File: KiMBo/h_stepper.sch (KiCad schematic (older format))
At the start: 24 parts, among them U18 TMC2130

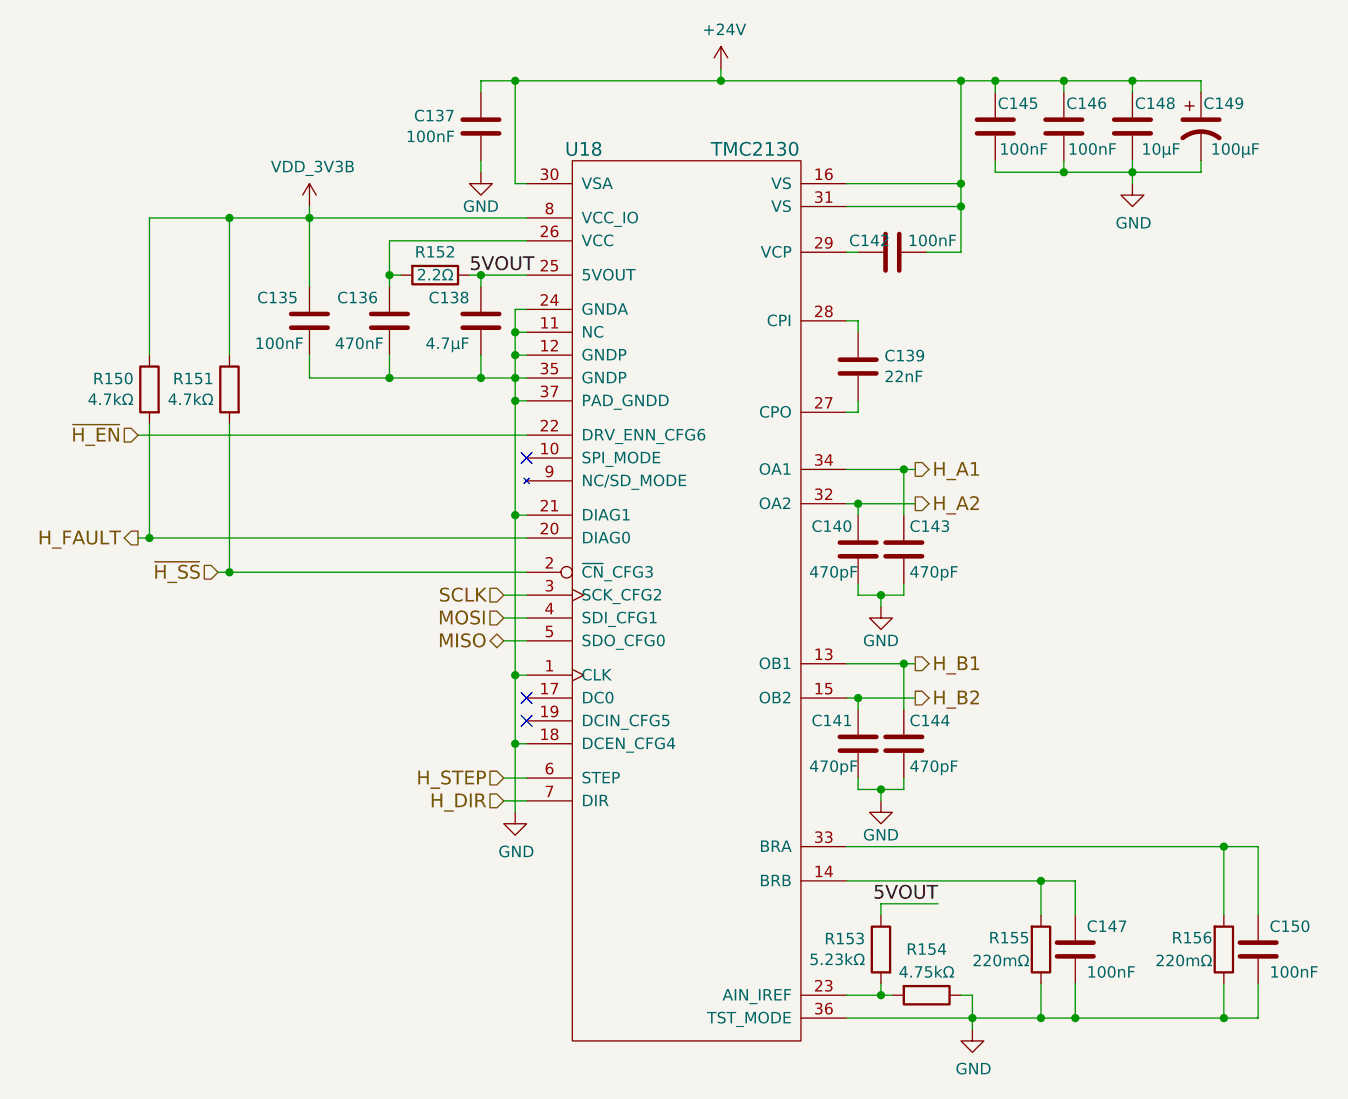
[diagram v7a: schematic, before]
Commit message: Remove the unneeded oscillator, track down which components are underneath the OSD3358 and put them on the top
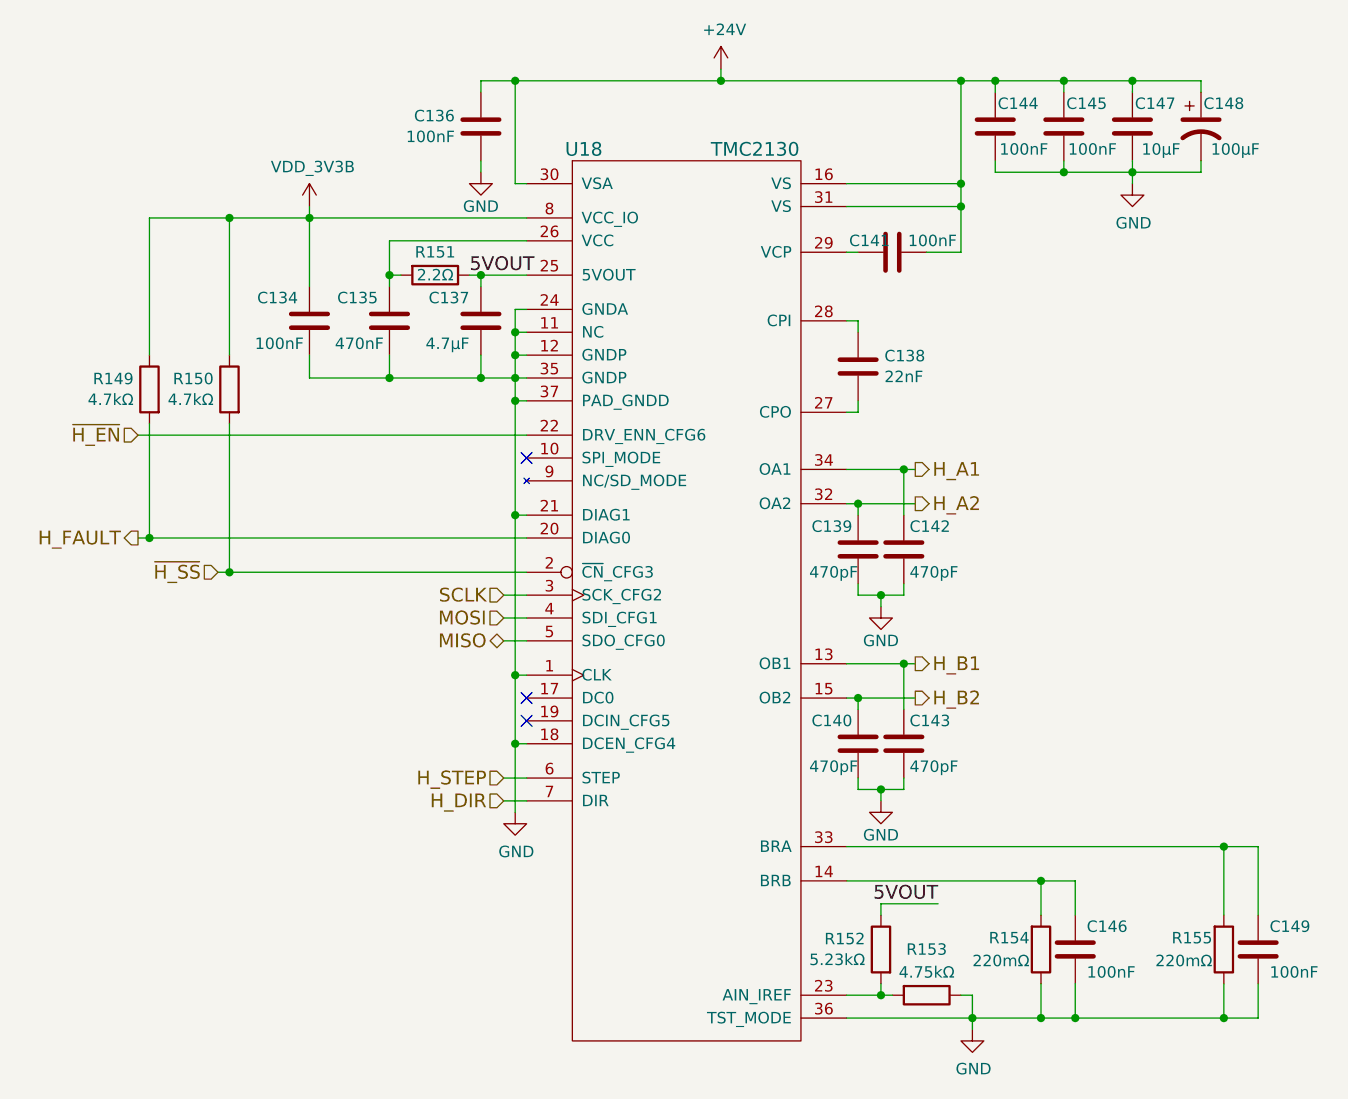
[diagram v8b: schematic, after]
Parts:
- renumbered C135 to C134, C136 to C135, C137 to C136, C138 to C137, C139 to C138, C140 to C139, C141 to C140, C142 to C141, C143 to C142, C144 to C143, C145 to C144, C146 to C145, C147 to C146, C148 to C147, C149 to C148, C150 to C149, R150 to R149, R151 to R150, R152 to R151, R153 to R152, R154 to R153, R155 to R154, R156 to R155
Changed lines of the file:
@@
 MOSI
 $Comp
-L C C137
+L C C136
 U 1 1 5BA7E11E
 P 7300 3950
-F 0 "C137" H 7186 3904 50  0000 R CNN
+F 0 "C136" H 7186 3904 50  0000 R CNN
 F 1 "100nF" H 7186 3995 50  0000 R CNN
 F 2 "Capacitors_SMD:C_0603" H 7338 3800 50  0001 C CNN
@@
 $EndComp
 $Comp
-L C C142
+L C C141
 U 1 1 589B8C70
 P 9100 4500
-F 0 "C142" V 9050 4400 50  0000 C CNN
+F 0 "C141" V 9050 4400 50  0000 C CNN
 F 1 "100nF" V 9050 4675 50  0000 C CNN
 F 2 "Capacitors_SMD:C_0603" H 9138 4350 50  0001 C CNN
@@
 $EndComp
 $Comp
-L CP1 C149
+L CP1 C148
 U 1 1 589B8CBD
 P 10450 3950
-F 0 "C149" H 10550 4050 50  0000 C CNN
+F 0 "C148" H 10550 4050 50  0000 C CNN
 F 1 "100μF" H 10600 3850 50  0000 C CNN
 F 2 "Capacitors_SMD:c_elec_8x10" H 10450 3950 50  0001 C CNN
@@
 $EndComp
 $Comp
-L C C145
+L C C144
 U 1 1 5BA7E121
 P 9550 3950
-F 0 "C145" H 9450 4050 50  0000 C CNN
+F 0 "C144" H 9450 4050 50  0000 C CNN
 F 1 "100nF" H 9425 3850 50  0000 C CNN
 F 2 "Capacitors_SMD:C_0603" H 9588 3800 50  0001 C CNN
@@
 $EndComp
 $Comp
-L GND #PWR0204
+L GND #PWR0202
 U 1 1 5BA7E122
 P 7300 4150
-F 0 "#PWR0204" H 7300 3900 50  0001 C CNN
+F 0 "#PWR0202" H 7300 3900 50  0001 C CNN
 F 1 "GND" H 7300 4000 50  0000 C CNN
 F 2 "" H 7300 4150 50  0000 C CNN
@@
 $EndComp
 $Comp
-L C C146
+L C C145
 U 1 1 5BA7E123
 P 9850 3950
-F 0 "C146" H 9750 4050 50  0000 C CNN
+F 0 "C145" H 9750 4050 50  0000 C CNN
 F 1 "100nF" H 9725 3850 50  0000 C CNN
 F 2 "Capacitors_SMD:C_0603" H 9888 3800 50  0001 C CNN
@@
 $EndComp
 $Comp
-L GND #PWR0205
+L GND #PWR0203
 U 1 1 5BA7E124
 P 10150 4200
-F 0 "#PWR0205" H 10150 3950 50  0001 C CNN
+F 0 "#PWR0203" H 10150 3950 50  0001 C CNN
 F 1 "GND" H 10155 4027 50  0000 C CNN
 F 2 "" H 10150 4200 50  0000 C CNN
@@
 $EndComp
 $Comp
-L +24V #PWR0206
+L +24V #PWR0204
 U 1 1 589BEDE1
 P 8350 3700
-F 0 "#PWR0206" H 8350 3550 50  0001 C CNN
+F 0 "#PWR0204" H 8350 3550 50  0001 C CNN
 F 1 "+24V" H 8365 3873 50  0000 C CNN
 F 2 "" H 8350 3700 50  0000 C CNN
@@
 $EndComp
 $Comp
-L C C139
+L C C138
 U 1 1 5BA7E126
 P 8950 5000
-F 0 "C139" H 9065 5046 50  0000 L CNN
+F 0 "C138" H 9065 5046 50  0000 L CNN
 F 1 "22nF" H 9065 4955 50  0000 L CNN
 F 2 "Capacitors_SMD:C_0603" H 8988 4850 50  0001 C CNN
@@
 $EndComp
 $Comp
-L R R156
+L R R155
 U 1 1 5BA7E127
 P 10550 7550
-F 0 "R156" H 10500 7500 50  0000 R CNN
+F 0 "R155" H 10500 7500 50  0000 R CNN
 F 1 "220mΩ" H 10500 7600 50  0000 R CNN
 F 2 "Resistors_SMD:R_0805" V 10480 7550 50  0001 C CNN
@@
 $EndComp
 $Comp
-L R R155
+L R R154
 U 1 1 5BA7E128
 P 9750 7550
-F 0 "R155" H 9700 7500 50  0000 R CNN
+F 0 "R154" H 9700 7500 50  0000 R CNN
 F 1 "220mΩ" H 9700 7600 50  0000 R CNN
 F 2 "Resistors_SMD:R_0805" V 9680 7550 50  0001 C CNN
@@
 $EndComp
 $Comp
-L GND #PWR0207
+L GND #PWR0205
 U 1 1 589C2B70
 P 9450 7900
-F 0 "#PWR0207" H 9450 7650 50  0001 C CNN
+F 0 "#PWR0205" H 9450 7650 50  0001 C CNN
 F 1 "GND" H 9455 7727 50  0000 C CNN
 F 2 "" H 9450 7900 50  0000 C CNN
@@
 NoConn ~ 7500 6450
 $Comp
-L R R152
+L R R151
 U 1 1 589C4ED8
 P 7100 4600
-F 0 "R152" V 7000 4600 50  0000 C CNN
+F 0 "R151" V 7000 4600 50  0000 C CNN
 F 1 "2.2Ω" V 7100 4600 50  0000 C CNN
 F 2 "Resistors_SMD:R_0603" V 7030 4600 50  0001 C CNN
@@
 $EndComp
 $Comp
-L C C136
+L C C135
 U 1 1 5BA7E12C
 P 6900 4800
-F 0 "C136" H 6950 4900 50  0000 L CNN
+F 0 "C135" H 6950 4900 50  0000 L CNN
 F 1 "470nF" H 6925 4700 50  0000 L CNN
 F 2 "Capacitors_SMD:C_0603" H 6938 4650 50  0001 C CNN
@@
 NoConn ~ 7500 6550
 $Comp
-L GND #PWR0208
+L GND #PWR0206
 U 1 1 5BA7E12D
 P 7450 6950
-F 0 "#PWR0208" H 7450 6700 50  0001 C CNN
+F 0 "#PWR0206" H 7450 6700 50  0001 C CNN
 F 1 "GND" H 7455 6777 50  0000 C CNN
 F 2 "" H 7450 6950 50  0000 C CNN
@@
 $EndComp
 $Comp
-L C C147
+L C C146
 U 1 1 589CC9B9
 P 9900 7550
-F 0 "C147" H 9950 7650 50  0000 L CNN
+F 0 "C146" H 9950 7650 50  0000 L CNN
 F 1 "100nF" H 9950 7450 50  0000 L CNN
 F 2 "Capacitors_SMD:C_0603" H 9938 7400 50  0001 C CNN
@@
 H_FAULT
 $Comp
-L R R150
+L R R149
 U 1 1 5BA7E12F
 P 5850 5100
-F 0 "R150" H 5919 5146 50  0000 L CNN
+F 0 "R149" H 5919 5146 50  0000 L CNN
 F 1 "4.7kΩ" H 5919 5055 50  0000 L CNN
 F 2 "Resistors_SMD:R_0603" V 5780 5100 50  0001 C CNN
@@
 NoConn ~ 7500 5400
 $Comp
-L C C138
+L C C137
 U 1 1 589C396E
 P 7300 4800
-F 0 "C138" H 7350 4900 50  0000 L CNN
+F 0 "C137" H 7350 4900 50  0000 L CNN
 F 1 "4.7μF" H 7350 4700 50  0000 L CNN
 F 2 "Capacitors_SMD:C_0603" H 7338 4650 50  0001 C CNN
@@
 5VOUT
 $Comp
-L R R153
+L R R152
 U 1 1 5BA7E130
 P 9050 7550
-F 0 "R153" H 9119 7596 50  0000 L CNN
+F 0 "R152" H 9119 7596 50  0000 L CNN
 F 1 "5.23kΩ" H 9119 7505 50  0000 L CNN
 F 2 "Resistors_SMD:R_0603" V 8980 7550 50  0001 C CNN
@@
 5VOUT
 $Comp
-L R R154
+L R R153
 U 1 1 5BA7E131
 P 9250 7750
-F 0 "R154" V 9050 7750 50  0000 C CNN
+F 0 "R153" V 9050 7750 50  0000 C CNN
 F 1 "4.75kΩ" V 9150 7750 50  0000 C CNN
 F 2 "Resistors_SMD:R_0603" V 9180 7750 50  0001 C CNN
@@
 $EndComp
 $Comp
-L R R151
+L R R150
 U 1 1 58A47723
 P 6200 5100
-F 0 "R151" H 6269 5146 50  0000 L CNN
+F 0 "R150" H 6269 5146 50  0000 L CNN
 F 1 "4.7kΩ" H 6269 5055 50  0000 L CNN
 F 2 "Resistors_SMD:R_0603" V 6130 5100 50  0001 C CNN
@@
 $EndComp
 $Comp
-L C C150
+L C C149
 U 1 1 58AF169E
 P 10700 7550
-F 0 "C150" H 10750 7650 50  0000 L CNN
+F 0 "C149" H 10750 7650 50  0000 L CNN
 F 1 "100nF" H 10750 7450 50  0000 L CNN
 F 2 "Capacitors_SMD:C_0603" H 10738 7400 50  0001 C CNN
@@
 $EndComp
 $Comp
-L C C140
+L C C139
 U 1 1 58B19CCF
 P 8950 5800
-F 0 "C140" H 8975 5900 50  0000 L CNN
+F 0 "C139" H 8975 5900 50  0000 L CNN
 F 1 "470pF" H 8950 5700 50  0000 L CNN
 F 2 "Capacitors_SMD:C_0603" H 8988 5650 50  0001 C CNN
@@
 $EndComp
 $Comp
-L GND #PWR0209
+L GND #PWR0207
 U 1 1 5BA7E135
 P 9050 6050
-F 0 "#PWR0209" H 9050 5800 50  0001 C CNN
+F 0 "#PWR0207" H 9050 5800 50  0001 C CNN
 F 1 "GND" H 9050 5900 50  0000 C CNN
 F 2 "" H 9050 6050 50  0000 C CNN
@@
 $EndComp
 $Comp
-L C C143
+L C C142
 U 1 1 5BA7E136
 P 9150 5800
-F 0 "C143" H 9175 5900 50  0000 L CNN
+F 0 "C142" H 9175 5900 50  0000 L CNN
 F 1 "470pF" H 9175 5700 50  0000 L CNN
 F 2 "Capacitors_SMD:C_0603" H 9188 5650 50  0001 C CNN
@@
 $EndComp
 $Comp
-L C C141
+L C C140
 U 1 1 5BA7E137
 P 8950 6650
-F 0 "C141" H 8975 6750 50  0000 L CNN
+F 0 "C140" H 8975 6750 50  0000 L CNN
 F 1 "470pF" H 8950 6550 50  0000 L CNN
 F 2 "Capacitors_SMD:C_0603" H 8988 6500 50  0001 C CNN
@@
 $EndComp
 $Comp
-L GND #PWR0210
+L GND #PWR0208
 U 1 1 5BA7E138
 P 9050 6900
-F 0 "#PWR0210" H 9050 6650 50  0001 C CNN
+F 0 "#PWR0208" H 9050 6650 50  0001 C CNN
 F 1 "GND" H 9050 6750 50  0000 C CNN
 F 2 "" H 9050 6900 50  0000 C CNN
@@
 $EndComp
 $Comp
-L C C144
+L C C143
 U 1 1 5BA7E139
 P 9150 6650
-F 0 "C144" H 9175 6750 50  0000 L CNN
+F 0 "C143" H 9175 6750 50  0000 L CNN
 F 1 "470pF" H 9175 6550 50  0000 L CNN
 F 2 "Capacitors_SMD:C_0603" H 9188 6500 50  0001 C CNN
@@
 	8950 6850 8950 6800
 $Comp
-L C C148
+L C C147
 U 1 1 5BA7E13A
 P 10150 3950
-F 0 "C148" H 10050 4050 50  0000 C CNN
+F 0 "C147" H 10050 4050 50  0000 C CNN
 F 1 "10μF" H 10025 3850 50  0000 C CNN
 F 2 "Capacitors_SMD:C_0805" H 10188 3800 50  0001 C CNN
@@
 	5850 4350 7500 4350
 $Comp
-L VDD_3V3B #PWR0211
+L VDD_3V3B #PWR0209
 U 1 1 5A2FEA7A
 P 6550 4300
-F 0 "#PWR0211" H 6550 4150 50  0001 C CNN
+F 0 "#PWR0209" H 6550 4150 50  0001 C CNN
 F 1 "VDD_3V3B" H 6565 4473 50  0000 C CNN
 F 2 "" H 6550 4300 50  0000 C CNN
@@
 $EndComp
 $Comp
-L C C135
+L C C134
 U 1 1 5A897FB1
 P 6550 4800
-F 0 "C135" H 6600 4900 50  0000 L CNN
+F 0 "C134" H 6600 4900 50  0000 L CNN
 F 1 "100nF" H 6575 4700 50  0000 L CNN
 F 2 "Capacitors_SMD:C_0603" H 6588 4650 50  0001 C CNN
